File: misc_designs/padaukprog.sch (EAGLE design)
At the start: 126 parts, among them IC1 LM358D, J1 JUMPER_SOLDER_1X2, M1 XT1861B, P1 B3B-PH-K, Q1 BSS84, Q2 8MHz, Q3 BSS84, Q4 BSS123, U1 MIC550X

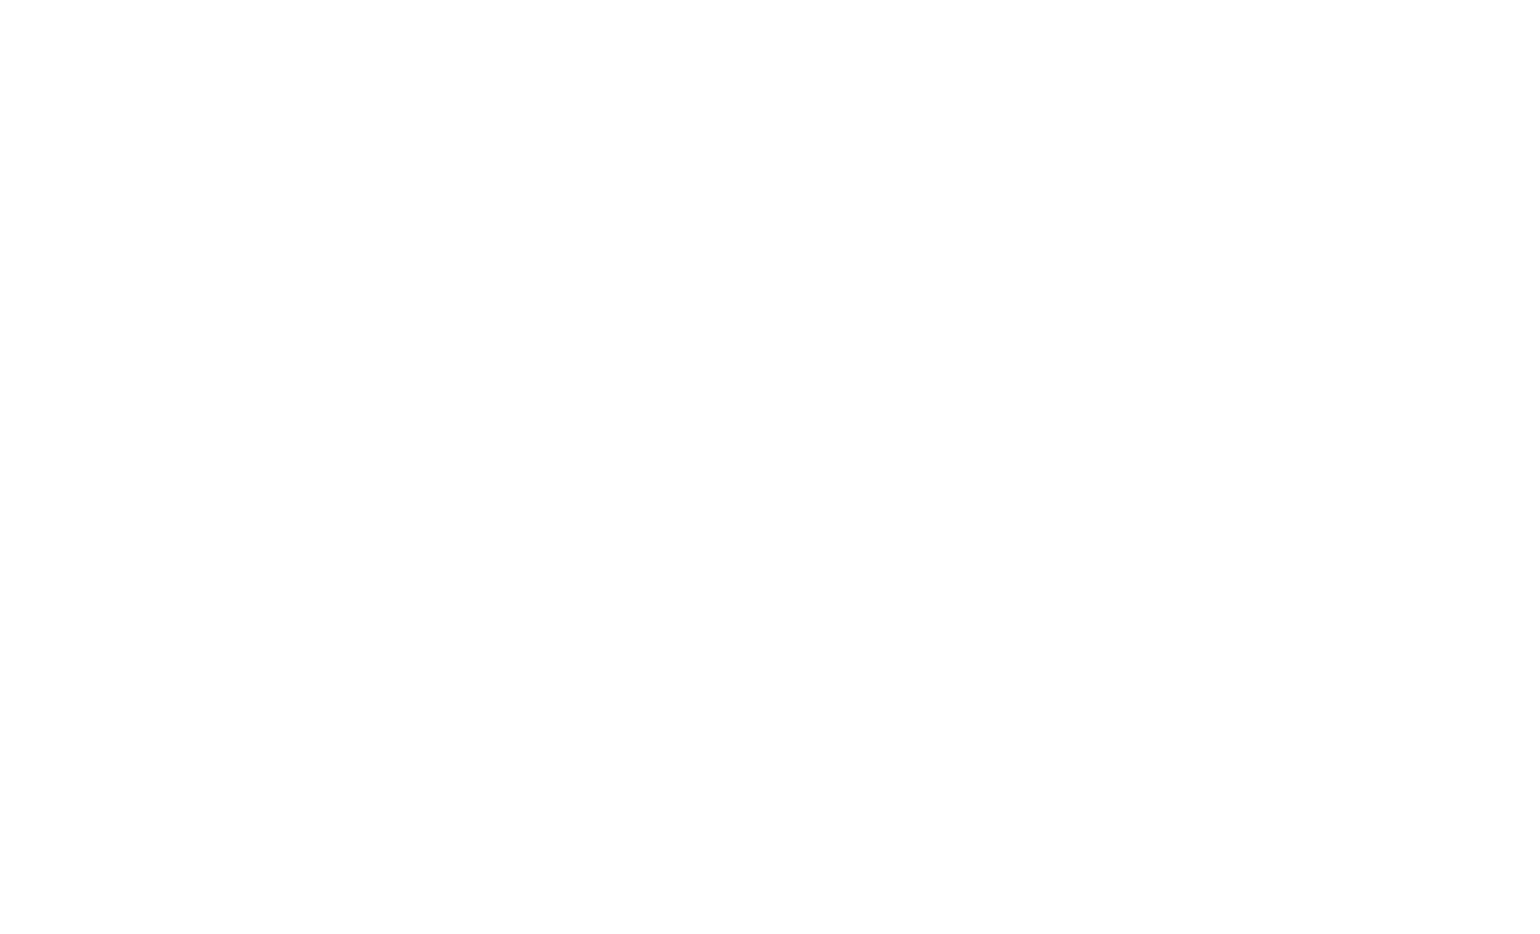
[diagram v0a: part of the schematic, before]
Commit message: Add minimal STM32F030
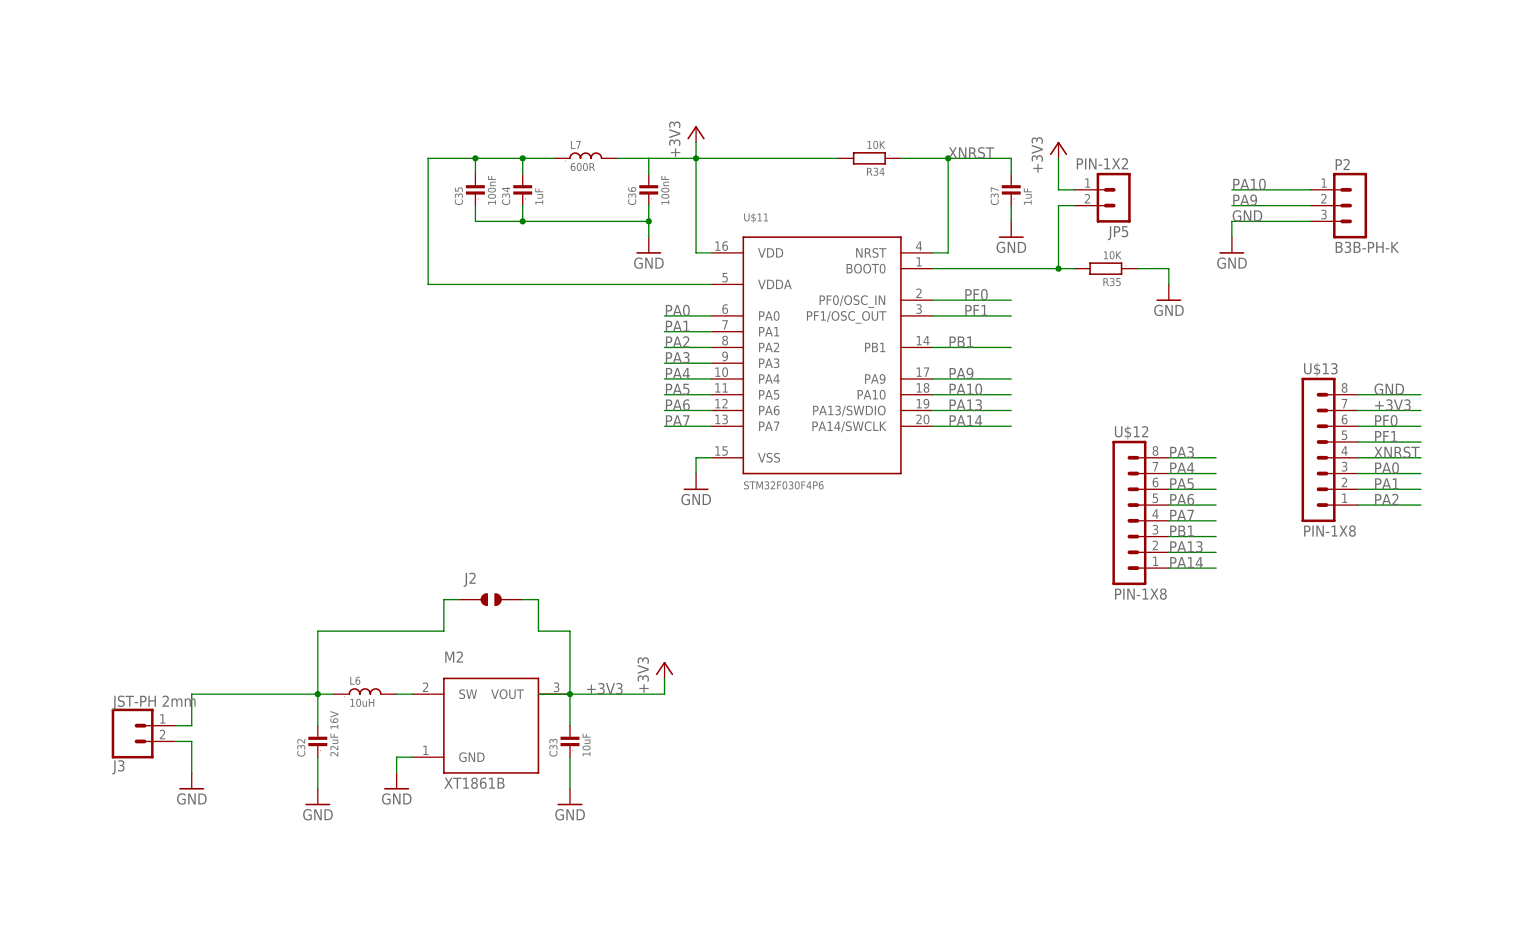
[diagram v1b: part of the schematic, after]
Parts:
- added C32: 22uF 16V, GadgetFactory:C0805
- added C33: 10uF, GadgetFactory:C0603
- added C34, C37: 1uF, GadgetFactory:C0603
- added C35, C36: 100nF, GadgetFactory:C0603
- added J2: JUMPER_SOLDER_1X2, dp_devices:JUMPER_SOLDER_1X2
- added J3: JST-PH 2mm, SparkFun-Connectors:CONN_02JST-PTH-2
- added JP5: PIN-1X2, alvie:PIN-1X2
- added L6: 10uH, GadgetFactory:L0805
- added L7: 600R, GadgetFactory:L0805
- added M2: XT1861B, alvie:XT1861B
- added P2: B3B-PH-K, con-jst-ph:B3B-PH-K
- added R34, R35: 10K, GadgetFactory:R0603
- added U$11: STM32F030F4P6, alvie:STM32F030F4P6
- added U$12, U$13: PIN-1X8, alvie:PIN-1X8
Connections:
- new net N$10: C34.2, C35.2, L7.1, U$11.VDDA
- new net N$13: C32.2, J2.1, J3.1, L6.1
- new net N$16: L6.2, M2.SW
- new net N$23: JP5.2, R35A.2, U$11.BOOT0
- new net PA0: U$11.PA0, U$13.3
- new net PA1: U$11.PA1, U$13.2
- new net PA10: P2.1, U$11.PA10
- new net PA13: U$11.PA13/SWDIO, U$12.2
- new net PA14: U$11.PA14/SWCLK, U$12.1
- new net PA2: U$11.PA2, U$13.1
- new net PA3: U$11.PA3, U$12.8
- new net PA4: U$11.PA4, U$12.7
- new net PA5: U$11.PA5, U$12.6
- new net PA6: U$11.PA6, U$12.5
- new net PA7: U$11.PA7, U$12.4
- new net PA9: P2.2, U$11.PA9
- new net PB1: U$11.PB1, U$12.3
- new net PF0: U$11.PF0/OSC_IN, U$13.6
- new net PF1: U$11.PF1/OSC_OUT, U$13.5
- new net XNRST: C37.2, R34A.1, U$11.NRST, U$13.4
- net +3V3: now also C33.2, C36.2, J2.2, JP5.1, L7.2, M2.VOUT, R34A.2, U$11.VDD, U$13.7
- net GND: now also C32.1, C33.1, C34.1, C35.1, C36.1, C37.1, J3.2, M2.GND, P2.3, R35A.1, U$11.VSS, U$13.8

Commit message: Updates
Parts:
- removed TP1, TP10, TP2, TP3, TP4, TP5, TP6, TP7, TP8, TP9: TPTP12SQ, testpad:TPTP12SQ
- added BOOT2, JP7: PIN-1X2, alvie:PIN-1X2
- added C38, C39: 16pF 6.3V, GadgetFactory:C0603
- added C40, C41, C42, C43, C45: 100nF 6.3V, GadgetFactory:C0603
- added C44, C46: 10uF, GadgetFactory:C0603
- added C47, C52: 20pF 6.3V, GadgetFactory:C0603
- added C48, C49, C55: 10uF, GadgetFactory:C0805
- added C50, C53, C54, C57, C58, C59, C60, C61, C93, C94, C95: 100nF, GadgetFactory:C0603
- added C51, C56: 10nF, GadgetFactory:C0603
- added C96: 2.2uF, GadgetFactory:C0805
- added C97: 1uF, GadgetFactory:C0603
- added C98: 1nF, GadgetFactory:C0603
- added C99: 100nF/DNP, GadgetFactory:C0603
- added D4: 1N4148W, alvie:1N4148W
- added H5, H7, H8: MOUNT-PAD-ROUND3.2, holes:MOUNT-PAD-ROUND3.2
- added IC11: LAN8720A, sigedi-footprints:LAN8720A
- added IC15: TPS62063, alvie:TPS62063
- added J4: (no value), GadgetFactory:JACK-PLUG
- added L10, L12, L9: 600R, GadgetFactory:L0805
- added L11: DFE252012F, alvie:DFE252012F
- added L8: 10mH, GadgetFactory:L0805
- added LED4, LED5, LED6: LG L29K-G2J1-24, dp_devices:LED-0603
- added Q5: 25MHz, crystal:CRYSTALHC49U-V
- added Q6: FDN338, transistor-power:FDN360P
- added Q7: 8MHz, crystal:CRYSTALHC49U-V
- added R36, R37, R39, R40: 20R, GadgetFactory:R0603
- added R38, R43, R50, R78: 10K, GadgetFactory:R0603
- added R41, R42, R53, R54, R55, R57, R60: 0R, GadgetFactory:R0603
- added R44: 100K, GadgetFactory:R0603
- added R45, R46, R47, R79, R80: 2K2, GadgetFactory:R0603
- added R48, R49: 2K2/DNP, GadgetFactory:R0603
- added R51: 1K5/DNP, GadgetFactory:R0603
- added R52: 470K, GadgetFactory:R0603
- added R56, R61: 0R/DNP, GadgetFactory:R0603
- added R58, R59: 330R, GadgetFactory:R0603
- added R82: 12K1, GadgetFactory:R0603
- added R83, R84, R85, R86: 49R9, GadgetFactory:R0603
- added S2, S3: SWITCHES_-SMD-1101NE, EAGLE_BoosterPack_Library:SWITCHES_-SMD-1101NE
- added SV1: (no value), con-lstb:MA13-2W
- added T2: Hanrun HR917550A, alvie:HR913550A
- added TP20, TP21, TP22, TP23, TP24, TP25, TP26, TP27, TP28, TP29: TPTP12SQ, testpad:TPTP12SQ
- added U$14: PN532_NFCB, alvie:PN532_NFCB
- added U$15: STM32F070F6, alvie:STM32F070F6
- added U$16: MIC550X, alvie:MIC550X
- added U$17: PIN-1X4, alvie:PIN-1X4
- added U2: STM32F107RCT6, ST Microelctronics_By_element14_Batch_1:STM32F107RCT6
- added U3: ESP-WROOM-32, esp32:ESP-WROOM-32
- added USB2, USB3: CON-USB-F-MICRO-B, dp_devices:CON-USB-F-MICRO-B
- U$10: value SOP-16-1.27 -> PIN-1X4; device alvie:SOP-16-1.27 -> alvie:PIN-1X4
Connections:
- removed net N$34: TP2.TP, U$10.2
- removed net N$38: TP3.TP, U$10.3
- removed net N$41: TP4.TP, U$10.4
- removed net N$47: TP9.TP, U$10.16
- removed net N$48: TP8.TP, U$10.15
- removed net N$49: TP7.TP, U$10.14
- removed net N$52: TP6.TP, U$10.13
- new net ESP_EN: U2.PA14, U3.EN
- new net ESP_IO0: U2.PC12, U3.IO0
- new net ESP_MISO: R56A.2, R57A.2, U3.IO19
- new net ESP_MOSI: R60A.2, R61A.2, U3.IO23
- new net ESP_ON: Q6.G, R44A.2
- new net ESP_RX: U2.PC10, U3.RXD0
- new net ESP_SCK: R55A.2, U3.IO18
- new net ESP_TX: U2.PC11, U3.TXD0
- new net ESP_VCC: Q6.D, U3.3V3
- new net MCO: R53A.1, U2.PA8
- new net N$17: L12.1, USB3USB.VUSB
- new net N$20: R39A.1, USB2USB.D-
- new net N$22: R40A.1, USB2USB.D+
- new net N$24: R42A.1, USB2USB.USBID
- new net N$25: R54A.2, U3.IO5
- new net N$26: LED4.C, R45A.1
- new net N$27: LED5.C, R46A.1
- new net N$28: LED6.C, R47A.1
- new net N$29: R36A.1, USB3USB.D-
- new net N$30: IC2.16, TP23.TP
- new net N$31: IC2.15, TP22.TP
- new net N$32: IC2.14, TP21.TP
- new net N$35: IC2.13, TP20.TP
- new net N$39: L9.1, USB2USB.VUSB
- new net N$40: IC11.RBIAS, R82A.2
- new net N$44: C57.1, T2G$1.5
- new net N$45: C58.1, T2G$1.4
- new net N$46: R58A.1, T2YELLOW.A
- new net N$53: R59A.1, T2GREEN.A
- new net N$54: IC2.1, TP24.TP
- new net N$55: IC2.2, TP25.TP
- new net N$56: C99.2, L10.2, R83A.2, R84A.2, R85A.2, R86A.2
- new net N$57: IC2.3, TP26.TP
- new net N$58: C97.2, C98.2, IC11.VDDCR
- new net N$59: IC2.4, TP27.TP
- new net NBOOT0: BOOT2.1, R38A.2, U$15.BOOT0
- new net NIRQ: U$14.IRQ, U$15.PA1
- new net NLED0: R45A.2, U2.PA13
- new net NLED1: R46A.2, U2.PB14
- new net NLED2: R47A.2, U2.PB15
- new net NNRST: R43A.1, S3.1, U$15.NRST
- new net NOSC_IN: C47.2, Q7.2, U$15.PF0/OSC_IN
- new net NOSC_OUT: C52.2, Q7.1, U$15.PF1/OSC_OUT
- new net NRSTO: U$14.RSTO, U$15.PA0
- new net NSWCLK: U$15.PA14, U$17.3
- new net NSWDIO: U$15.PA13, U$17.2
- new net NUSBDM: R36A.2, U$15.PA9/PA11
- new net NUSBDP: R37A.2, R51A.1, U$15.PA10/PA12
- new net N_MISO: U$14.MISO, U$15.PA6
- new net N_MOSI: U$14.MOSI, U$15.PA7
- new net N_RX: U$14.SDA/TX, U$15.PA3
- new net N_SCK: U$14.SCK, U$15.PA5
- new net N_SS: U$14.SS, U$15.PA4
- new net N_TX: U$14.SCL/RX, U$15.PA2
- new net PA15/NSS: R54A.1, U2.PA15
- new net PA3/ADC3: SV1.9, U2.PA3
- new net PA4/DAC1: SV1.7, U2.PA4
- new net PA5/DAC2: SV1.8, U2.PA5
- new net PB6/UART1_TX: SV1.24, U2.PB6
- new net PB7/UART1_RX: SV1.23, U2.PB7
- new net PHY_LED0: IC11.LED1/REGOFF, T2GREEN.K
- new net PHY_LED1: IC11.LED2/NINTSEL, T2YELLOW.K
- new net REG33IN: C49.2, D4.C, IC15.AVIN, IC15.EN, IC15.PVIN, J4.3, SV1.2
- new net RMII_CRS_DV: IC11.CRS_DV/MODE2, U2.PA7
- new net RMII_MDC: IC11.MDC, R79A.1, U2.PC1
- new net RMII_MDIO: IC11.MDIO, R80A.1, U2.PA2
- new net RMII_NRST: IC11.NRST, R78A.1, U2.PA6
- new net RMII_REF_CLK: IC11.NINT/REFCLK0, U2.PA1
- new net RMII_RXD0: IC11.RXD0/MODE0, U2.PC4
- new net RMII_RXD1: IC11.RXD1/MODE1, U2.PC5
- new net RMII_TXD0: IC11.TXD0, U2.PB12
- new net RMII_TXD1: IC11.TXD1, U2.PB13
- new net RMII_TX_EN: IC11.TXEN, U2.PB11
- new net RXM1: IC11.TXN, R84A.1, T2G$1.2
- new net RXP1: IC11.TXP, R83A.1, T2G$1.1
- new net SHIELD: T2G$1.8, T2G$4.SHIELD
- new net TXM1: IC11.RXN, R86A.1, T2G$1.6
- new net TXP1: IC11.RXP, R85A.1, T2G$1.3
- new net USBID/UART1RX: R42A.2, U2.PA10
- new net USBPWR: D4.A, L9.2, R41A.1
- new net USBPWR1: C55.2, L12.2, U$16.EN, U$16.VIN
- new net VBUSDET/UART1TX: R41A.2, U2.PA9
- new net XBOOT0: JP7.1, R50A.1, U2.BOOT0
- new net XI: IC11.XTAL1/CLKIN, R53A.2
- new net XOSC_IN: C38.2, Q5.2, U2.PD0_OSC_IN
- new net XOSC_OUT: C39.2, Q5.1, U2.PD1_OSC_OUT
- new net XPA0: SV1.12, U2.PA0-WKUP
- new net XPB0/ADC8: SV1.10, U2.PB0
- new net XPB1: SV1.5, U2.PB1
- new net XPB2: SV1.6, U2.PB2
- new net XPC0: SV1.13, U2.PC0
- new net XPC13: SV1.22, U2.PC13-TAMPER-RTC
- new net XPC14: SV1.19, U2.PC14-OSC32_IN
- new net XPC15: SV1.20, U2.PC15-OSC32_OUT
- new net XPC2: SV1.14, U2.PC2
- new net XPC3: SV1.11, U2.PC3
- new net XPC6: SV1.15, U2.PC6
- new net XPC7: SV1.16, U2.PC7
- new net XPC8: SV1.17, U2.PC8
- new net XPC9: SV1.18, U2.PC9
- new net XPD2: SV1.21, U2.PD2
- new net XSCL: R48A.1, SV1.26, U$10.3, U2.PB8
- new net XSDA: R49A.1, SV1.25, U$10.4, U2.PB9
- new net XSPI_MISO: R57A.1, R61A.1, U2.PB4
- new net XSPI_MOSI: R56A.1, R60A.1, U2.PB5
- new net XSPI_SCK: R55A.1, U2.PB3
- new net XSW: IC15.SW, L11.1
- new net XUSBDM: R39A.2, U2.PA11
- new net XUSBDP: R40A.2, U2.PA12
- new net XVDDA: C40.1, C44.2, L8.2, U2.VDDA
- new net XXNRST: R52A.2, S2.2, U2.NRST
- net +3V3: now also BOOT2.2, C41.1, C42.1, C43.1, C45.1, C46.2, C48.2, C50.2, C51.2, C53.2, C54.2, C56.2, C59.2, C60.2, C61.2, C93.2, C94.2, C95.2, C96.2, IC11.VDD1A, IC11.VDD2A, IC11.VDDIO, IC15.FB, JP7.2, L10.1, L11.2, L8.1, LED4.A, LED5.A, LED6.A, Q6.S, R43A.2, R44A.1, R48A.2, R49A.2, R51A.2, R52A.1, R58A.2, R59A.2, R78A.2, R79A.2, R80A.2, SV1.1, U$10.2, U$14.VCC, U$15.VDD, U$15.VDDA, U$16.VOUT, U$17.1, U2.VBAT, U2.VDD_1, U2.VDD_2, U2.VDD_3, U2.VDD_4
- net GND: now also C38.1, C39.1, C40.2, C41.2, C42.2, C43.2, C44.1, C45.2, C46.1, C47.1, C48.1, C49.1, C50.1, C51.1, C52.1, C53.1, C54.1, C55.1, C56.1, C57.2, C58.2, C59.1, C60.1, C61.1, C93.1, C94.1, C95.1, C96.1, C97.1, C98.1, C99.1, IC11.VSS, IC15.AGND, IC15.MODE, IC15.PGND, J4.1, R38A.1, R50A.2, R82A.1, S2.1, S3.2, SV1.3, SV1.4, U$10.1, U$14.GND, U$15.VSS, U$16.GND, U$17.4, U2.VSSA, U2.VSS_1, U2.VSS_2, U2.VSS_3, U2.VSS_4, U3.GND, U3.GND@1, U3.GND@15, U3.GND@38, USB2USB.GND, USB3USB.GND; no longer U$10.12
- net MCU_MISO: no longer U$10.7
- net MCU_MOSI: no longer U$10.10
- net MCU_PA0: now also TP28.TP; no longer TP10.TP, U$10.11
- net MCU_PA7: now also TP29.TP; no longer TP5.TP, U$10.6
- net MCU_SCK: no longer U$10.9
- net N$33: now also R37A.1, USB3USB.D+; no longer TP1.TP, U$10.1
- net VDD_OUT: no longer U$10.5
- net VPP_OUT: no longer U$10.8
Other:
- note added: "Ethernet PHY, Magnetics"
- note added: "OLED"
- note added: "REVER load"
- note added: "USB connector"
- moved on the sheet: C15, C18, C19, R6, S1

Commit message: Wip for Zigbee
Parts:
- added C62, C63, C64: (no value), GadgetFactory:C0603
- added C65, C69, C83: (no value), GadgetFactory:C0805
- added C66: 22uF 16V, GadgetFactory:C0805
- added C67: 10uF, GadgetFactory:C0603
- added C68, C75: 100nF, GadgetFactory:C0603
- added C70, C71, C72, C73, C74: (no value), GadgetFactory:C0402
- added C76, C82: 1uF, GadgetFactory:C0603
- added C77, C78, C80, C81: 100nF, GadgetFactory:C0402
- added C79: 220pF, GadgetFactory:C0402
- added C84, C85, C86, C87: 15pF, GadgetFactory:C0402
- added IC4, IC5: 4051D, 40xx:4051D
- added IC6: IC_DIL16-SOIC-16, dp_devices:IC_DIL16-SOIC-16
- added J5: AVR_SPI_PRG_6NS, SparkFun-Connectors:AVR_SPI_PRG_6NS
- added J6: JST-PH 2mm, SparkFun-Connectors:CONN_02JST-PTH-2
- added J7: CON-HIROSE-COAXIAL-U.FL, m-pad-2.1:CON-HIROSE-COAXIAL-U.FL
- added JP10, JP8, U$26: PIN-1X8, alvie:PIN-1X8
- added JP11: PIN-1X2, alvie:PIN-1X2
- added JP6: VBat +, alvie:PIN-1X2
- added JP9: Pedal, alvie:PIN-1X2
- added L13: 10uH, GadgetFactory:L0805
- added L14, L15: (no value), GadgetFactory:L0402
- added L16: 600R, GadgetFactory:L0805
- added LED7, LED8: LG L29K-G2J1-24, dp_devices:LED-0603
- added M3: XT1861B, alvie:XT1861B
- added Q10, Q11, Q8, Q9: BSS84, transistor-small-signal:BSS84
- added Q12, Q13: CRISTAL-3225, alvie:CRISTAL-3225
- added R62, R63, R64, R65, R66, R87: 10K, GadgetFactory:R0603
- added R67, R68, R69, R70, R71, R72, R73, R74: 330R, GadgetFactory:R0603
- added R75: 56K, GadgetFactory:R0603
- added R76: 0R, GadgetFactory:R0603
- added R77, R81: 2K2, GadgetFactory:R0603
- added SJ1: SOLDERJUMPERNC, headers:SOLDERJUMPERNC
- added U$25: SR410361N, alvie:SR410361N
- added U$27: TSSOP16, alvie:TSSOP16
- added U$28: PFS154-S16, alvie:PFS154-S16
- added U$29, U$31, U$32, U$33: PIN-1X4, alvie:PIN-1X4
- added U$30: CC2530, alvie:CC2530
- added U4: ATTINY24A-SSU, Atmel_By_element14_Batch_1-00:ATTINY24A-SSU
- SV1: value (none) -> MA13-2W; device con-lstb:MA13-2W -> alvie:MA13-2W
- U$7: value PMS150C-S08 -> PIN-1X8; device alvie:PMS150C-S08 -> alvie:PIN-1X8
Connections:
- removed net USBID/UART1RX: R42A.2, U2.PA10
- removed net VBUSDET/UART1TX: R41A.2, U2.PA9
- removed net XPC8: SV1.17, U2.PC8
- removed net XPC9: SV1.18, U2.PC9
- removed net XPD2: SV1.21, U2.PD2
- new net +3V3_CC: C75.2, C76.2, C77.2, C78.2, C79.2, C80.2, C81.2, C83.2, L16.2, R87A.1, U$30G$2.AVDD1, U$30G$2.AVDD2, U$30G$2.AVDD3, U$30G$2.AVDD4, U$30G$2.AVDD5, U$30G$2.AVDD6, U$30G$2.DVDD1, U$30G$2.DVDD2, U$31.4
- new net A_MISO: J5.1, U4.PA5
- new net A_MOSI: J5.4, U4.PA6
- new net A_RESET: J5.5, U4.PB3
- new net A_SCK: J5.3, U4.PA4
- new net CA0: Q8.G, R63A.1, U$28.PA6
- new net CA1: Q9.G, R64A.1, U$28.PA7
- new net CA2: Q10.G, R65A.1, U$28.PB7
- new net CA3: Q11.G, R66A.1, U$28.PB6
- new net CCLED1: R77A.2, U$30G$1.P1_0
- new net CCLED2: R81A.2, U$30G$1.P1_1
- new net CC_MISO: R76A.2, U$30G$1.P1_7
- new net CC_MOSI: R42A.2, U$30G$1.P1_6
- new net CC_RST: R87A.2, U$30G$1.RESET_N, U2.PC8
- new net CC_RX: U$30G$1.P0_2, U2.PC12
- new net CC_SCK: R41A.2, U$30G$1.P1_5
- new net CC_SS: U$30G$1.P1_4, U2.PC9
- new net CC_TX: U$30G$1.P0_3, U2.PD2
- new net DEBUG_C: U$30G$1.P2_2, U$31.2
- new net DEBUG_D: U$30G$1.P2_1, U$31.3
- new net LCLK: U$28.PA0, U$29.2
- new net LDAT: U$28.PB0, U$29.3
- new net N$100: IC6.13, U$26.5, U$27.12
- new net N$101: IC6.14, U$26.6, U$27.11
- new net N$102: IC6.12, U$26.4, U$27.13
- new net N$103: IC6.11, U$26.3, U$27.14
- new net N$104: IC6.10, U$26.2, U$27.15
- new net N$105: IC6.9, U$26.1, U$27.16
- new net N$106: C85.2, Q12.1, U$30G$1.P2_4/XOSC32K_Q1
- new net N$34: IC4A.X, IC5A.X
- new net N$38: IC4A.X7, JP8.1
- new net N$41: C66.2, J6.1, L13.1
- new net N$47: L13.2, M3.SW
- new net N$48: C67.2, JP11.1, M3.VOUT
- new net N$49: IC5A.X0, JP10.8
- new net N$52: IC4A.X0, JP8.8
- new net N$60: IC4A.X1, JP8.7
- new net N$61: IC4A.X3, JP8.5
- new net N$62: IC4A.X4, JP8.4
- new net N$63: IC4A.X5, JP8.3
- new net N$64: IC4A.X6, JP8.2
- new net N$65: Q9.D, U$25.CA1
- new net N$66: J5.2, SJ1.2
- new net N$67: IC5A.X1, JP10.7
- new net N$68: IC5A.X2, JP10.6
- new net N$69: IC5A.X3, JP10.5
- new net N$70: IC4A.X2, JP8.6
- new net N$71: IC5A.X4, JP10.4
- new net N$72: IC5A.X5, JP10.3
- new net N$73: IC5A.X6, JP10.2
- new net N$74: IC5A.X7, JP10.1
- new net N$75: Q10.D, U$25.CA2
- new net N$76: Q8.D, U$25.CA0
- new net N$77: Q11.D, U$25.CA3
- new net N$78: C70.1, U$30G$3.RF_N
- new net N$79: C70.2, C73.2, L15.1
- new net N$80: C71.1, U$30G$3.RF_P
- new net N$81: IC6.8, U$27.1, U$7.1
- new net N$82: C71.2, C72.2, L14.1
- new net N$83: C73.1, C74.2, L14.2
- new net N$84: C74.1, J7.1
- new net N$85: R75A.2, U$30G$3.RBIAS
- new net N$86: C82.2, U$30G$2.DCOUPL
- new net N$87: LED8.C, R81A.1
- new net N$88: C86.2, Q13.3, U$30G$3.XOSC_Q2
- new net N$89: C87.2, Q13.1, U$30G$3.XOSC_Q1
- new net N$90: C84.2, Q12.3, U$30G$1.P2_3/XOSC32K_Q2
- new net N$91: IC6.7, U$27.2, U$7.2
- new net N$92: IC6.6, U$27.3, U$7.3
- new net N$93: IC6.5, U$27.4, U$7.4
- new net N$94: IC6.4, U$27.5, U$7.5
- new net N$95: IC6.3, U$27.6, U$7.6
- new net N$96: IC6.2, U$27.7, U$7.7
- new net N$97: IC6.1, U$27.8, U$7.8
- new net N$98: IC6.16, U$26.8, U$27.9
- new net N$99: IC6.15, U$26.7, U$27.10
- new net PEDAL: JP9.2, R62A.1, U4.PB2
- new net SA: R67A.2, U$25.A
- new net SB: R68A.2, U$25.B
- new net SC: R69A.2, U$25.C
- new net SD: R70A.2, U$25.D
- new net SDP: R74A.2, U$25.DP
- new net SE: R71A.2, U$25.E
- new net SEG_A: R67A.1, U$28.PA3
- new net SEG_B: R68A.1, U$28.PB1
- new net SEG_C: R69A.1, U$28.PB5
- new net SEG_D: R70A.1, U$28.PB2
- new net SEG_DP: R74A.1, U$28.PB3
- new net SEG_E: R71A.1, U$28.PA4
- new net SEG_F: R72A.1, U$28.PA5
- new net SEG_G: R73A.1, U$28.PB4
- new net SEL_A0: IC5A.A, U4.PA3
- new net SEL_A1: IC4A.A, U4.PA0
- new net SEL_B0: IC5A.B, U4.PA7
- new net SEL_B1: IC4A.B, U4.PA1
- new net SEL_C0: IC5A.C, U4.PB0
- new net SEL_C1: IC4A.C, U4.PA2
- new net SEL_INH: IC4A.INH, IC5A.INH, U4.PB1
- new net SF: R72A.2, U$25.F
- new net SG: R73A.2, U$25.G
- new net UART1RX: SV1.18, U2.PA10
- new net UART1TX: SV1.17, U2.PA9
- new net V_BATT: C62.1, C63.1, C64.1, C65.2, IC4P.VCC, IC5P.VCC, JP6.2, R62A.2, SJ1.1, U4.VCC
- net +3V3: now also C68.2, C69.2, L16.1, LED7.A, LED8.A, Q10.S, Q11.S, Q8.S, Q9.S, R63A.2, R64A.2, R65A.2, R66A.2, U$28.VCC, U$29.4, U$33.1
- net ESP_IO0: now also U2.PB10; no longer U2.PC12
- net ESP_MISO: now also R76A.1
- net ESP_MOSI: now also R42A.1
- net ESP_SCK: now also R41A.1
- net GND: now also C62.2, C63.2, C64.2, C65.1, C66.1, C67.1, C68.1, C69.1, C72.1, C75.1, C76.1, C77.1, C78.1, C79.1, C80.1, C81.1, C82.1, C83.1, C84.1, C85.1, C86.1, C87.1, IC4P.GND, IC4P.VEE, IC5P.GND, IC5P.VEE, J5.6, J6.2, J7.2, JP11.2, JP6.1, JP9.1, L15.2, M3.GND, Q12.2, Q12.4, Q13.2, Q13.4, R75A.1, U$28.GND, U$29.1, U$30G$2.GND, U$30G$2.GND@1, U$30G$2.GND@2, U$30G$2.GND@3, U$30G$2.PAD, U$31.1, U$32.1, U4.GND; no longer U$7.GND
- net MCU_MISO: no longer U$7.PA6
- net MCU_MOSI: no longer U$7.PA4
- net MCU_PA0: no longer U$7.PA0
- net MCU_PA7: no longer U$7.PA7
- net MCU_SCK: no longer U$7.PA3
- net N$24: now also LED7.C, R77A.1; no longer R42A.1, USB2USB.USBID
- net PA3/ADC3: now also U$33.2; no longer SV1.9
- net PA4/DAC1: now also U$33.3; no longer SV1.7
- net PA5/DAC2: now also U$32.3; no longer SV1.8
- net USBPWR: no longer R41A.1
- net VDD_OUT: no longer U$7.VCC
- net VPP_OUT: no longer U$7.PA5
- net XPB0/ADC8: now also U$32.2; no longer SV1.10
- net XPB1: now also U$33.4; no longer SV1.5
- net XPB2: now also U$32.4; no longer SV1.6
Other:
- note added: "15mA"
- note added: "2V"
- note added: "pa_ce"
- note added: "pa_tx_rx"
- moved on the sheet: R41, R42, U$7
